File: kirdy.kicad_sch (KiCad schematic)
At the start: 14 parts, among them J11 BG050-10A-0-0650-0737-0350-L-D, J12 Kirdy LD Adapter, J13 BG050-10A-0-0650-0737-0350-L-D

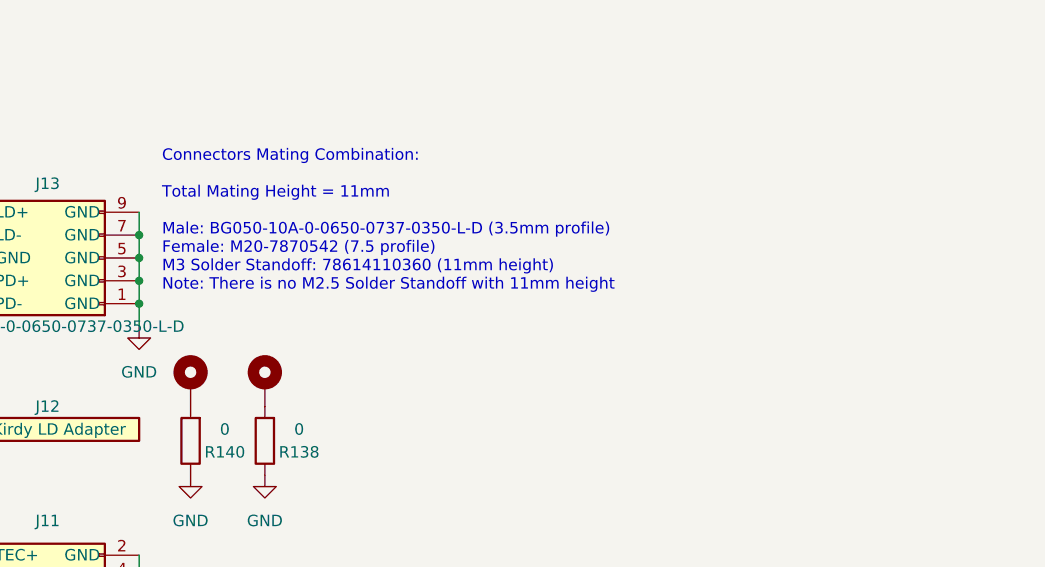
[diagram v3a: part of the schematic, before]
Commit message: sch, pcb: Add 12V & Mounting holes to MCU EXT HDR
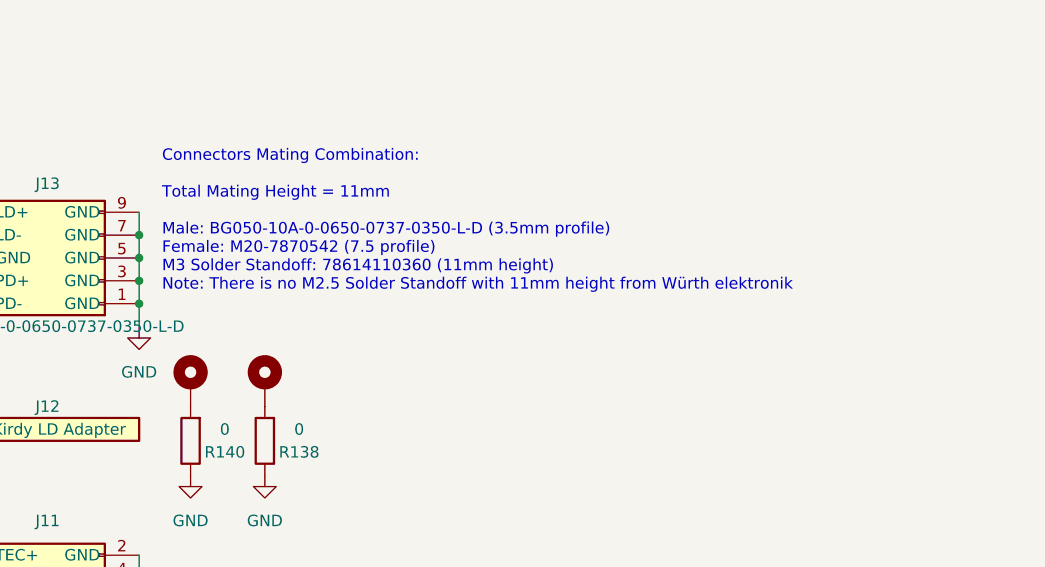
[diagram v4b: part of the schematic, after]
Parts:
- J11, J13: MFR_PN_ALT (none) -> BG050-10A-0-0450-0737-0350-L-D
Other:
- note added: "Connectors Mating Combination: Total Mating Height = 11mm Male: BG050-10A-0-0650-0737-0350-L-D (3.5mm profile) Female: M20-7870542 (7.5 profile) M3 Solder Standoff: 78614110360 (11mm height) Note: There is no M2.5 Solder Standoff with 11mm height from Würth elektronik"
- note removed: "Connectors Mating Combination: Total Mating Height = 11mm Male: BG050-10A-0-0650-0737-0350-L-D (3.5mm profile) Female: M20-7870542 (7.5 profile) M3 Solder Standoff: 78614110360 (11mm height) Note: There is no M2.5 Solder Standoff with 11mm height"
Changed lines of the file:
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@@
     (effects (font (size 2.54 2.54)) (justify left bottom))
   )
-  (text "Connectors Mating Combination:\n\nTotal Mating Height = 11mm\n\nMale: BG050-10A-0-0650-0737-0350-L-D (3.5mm profile) \nFemale: M20-7870542 (7.5 profile) \nM3 Solder Standoff: 78614110360 (11mm height)\nNote: There is no M2.5 Solder Standoff with 11mm height"
+  (text "Connectors Mating Combination:\n\nTotal Mating Height = 11mm\n\nMale: BG050-10A-0-0650-0737-0350-L-D (3.5mm profile) \nFemale: M20-7870542 (7.5 profile) \nM3 Solder Standoff: 78614110360 (11mm height)\nNote: There is no M2.5 Solder Standoff with 11mm height from Würth elektronik"
     (at 307.34 121.92 0)
     (effects (font (size 1.27 1.27)) (justify left bottom))
@@
     )
     (property "MFR_PN" "BG050-10A-0-0650-0737-0350-L-D" (at 304.8 123.19 0)
+      (effects (font (size 1.27 1.27)) hide)
+    )
+    (property "MFR_PN_ALT" "BG050-10A-0-0450-0737-0350-L-D " (at 304.8 123.19 0)
       (effects (font (size 1.27 1.27)) hide)
     )
@@
       (effects (font (size 1.27 1.27)) hide)
     )
+    (property "MFR_PN_ALT" "BG050-10A-0-0450-0737-0350-L-D " (at 284.48 151.13 0)
+      (effects (font (size 1.27 1.27)) hide)
+    )

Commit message: Cleanup and Update Modification Date
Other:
- note added: "Connectors Mating Combination: Total Mating Height = 11mm Male: BG050-10A-0-0650-0737-0350-L-D (3.5mm profile) Female: M20-7870542 (7.5mm profile) M3 Solder Standoff: 78614110360 (11mm height)"
- note removed: "Connectors Mating Combination: Total Mating Height = 11mm Male: BG050-10A-0-0650-0737-0350-L-D (3.5mm profile) Female: M20-7870542 (7.5 profile) M3 Solder Standoff: 78614110360 (11mm height) Note: There is no M2.5 Solder Standoff with 11mm height from Würth elektronik"
- note removed: "ToDo: Check all C0G New Tantalum footprints"
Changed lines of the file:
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@@
   (title_block
     (title "Kirdy")
-    (date "2023-11-09")
+    (date "2023-11-27")
     (rev "r0_3")
     (company "M-Labs Limited")
@@
     (stroke (width 0) (type default))
   )
-  (text "ToDo:\nCheck all C0G New Tantalum footprints" (at 216.535 53.975 0)
-    (effects (font (size 2.54 2.54)) (justify left bottom))
-  )
-  (text "Connectors Mating Combination:\n\nTotal Mating Height = 11mm\n\nMale: BG050-10A-0-0650-0737-0350-L-D (3.5mm profile) \nFemale: M20-7870542 (7.5 profile) \nM3 Solder Standoff: 78614110360 (11mm height)\nNote: There is no M2.5 Solder Standoff with 11mm height from Würth elektronik"
-    (at 307.34 121.92 0)
+  (text "Connectors Mating Combination:\n\nTotal Mating Height = 11mm\n\nMale: BG050-10A-0-0650-0737-0350-L-D (3.5mm profile) \nFemale: M20-7870542 (7.5mm profile) \nM3 Solder Standoff: 78614110360 (11mm height)"
+    (at 307.34 123.825 0)
     (effects (font (size 1.27 1.27)) (justify left bottom))
   )

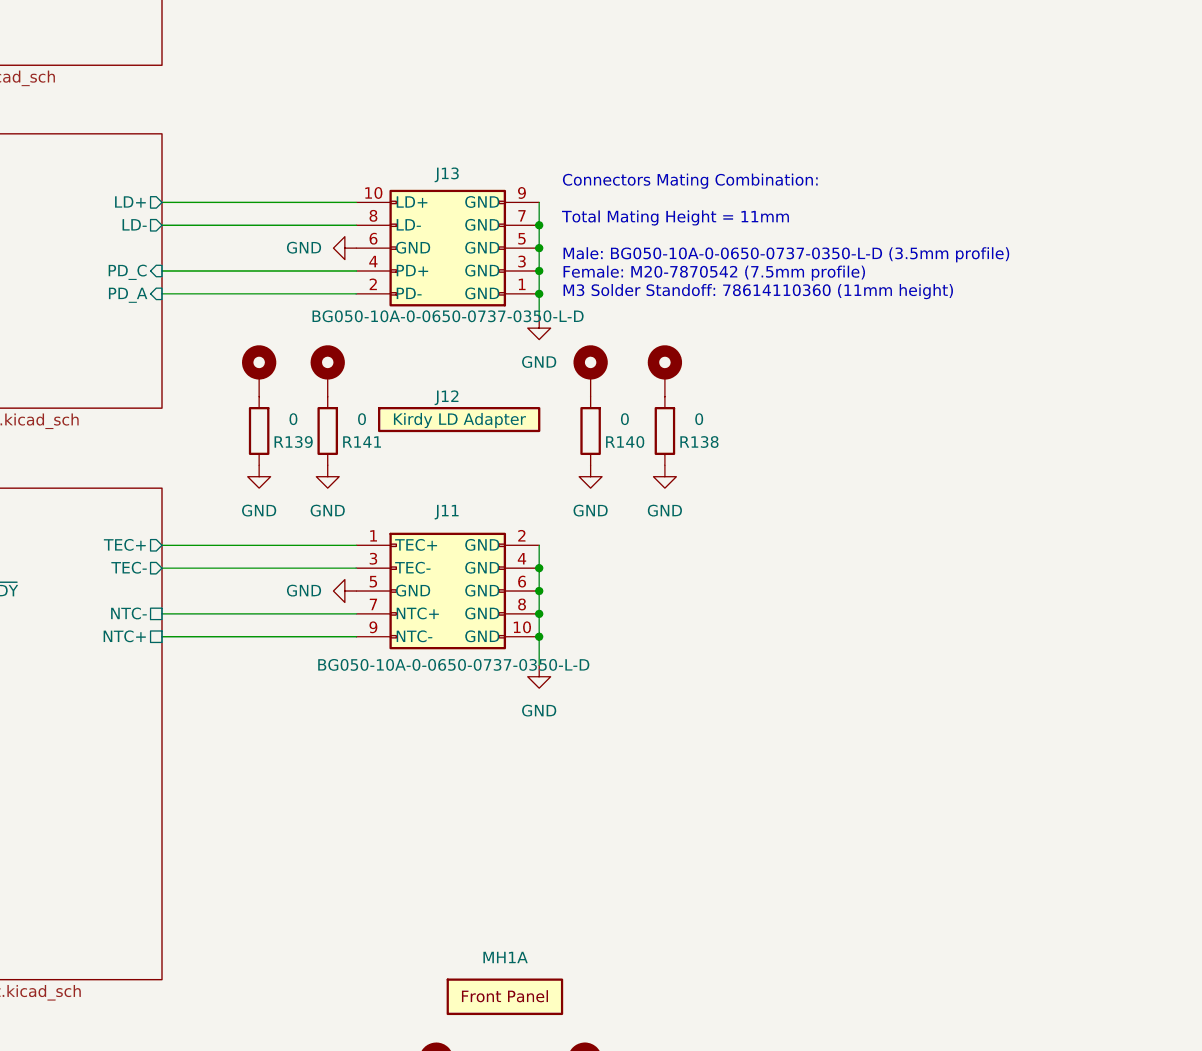
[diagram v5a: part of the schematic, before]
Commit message: sch: Add Mounting Screw Symbol and MFR/PN
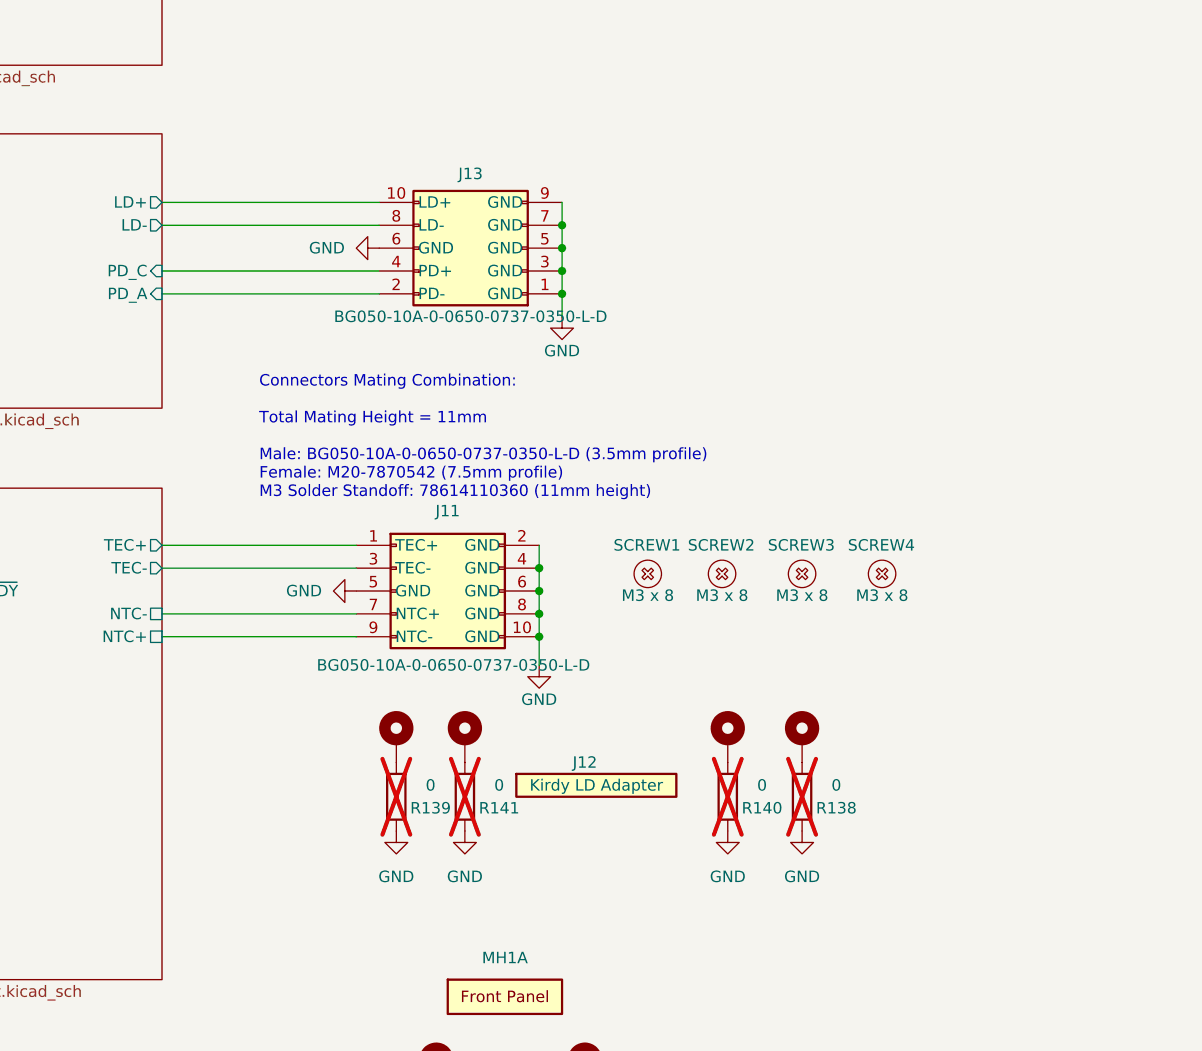
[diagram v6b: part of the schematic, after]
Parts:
- added SCREW1, SCREW2, SCREW3, SCREW4: M3 x 8, symbol kirdy:Screw
- R138, R139, R140, R141: now not fitted
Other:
- moved on the sheet: J12, J13

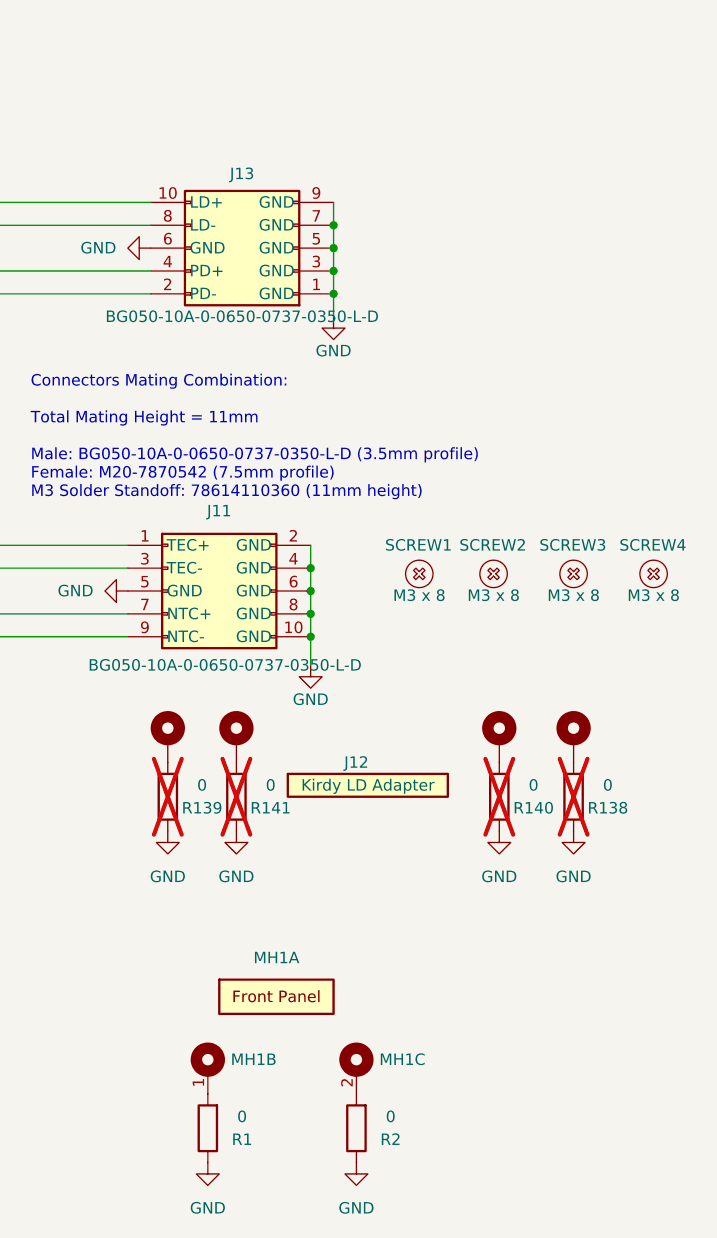
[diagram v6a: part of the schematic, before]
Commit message: Reassign Reference Designators for all Symbols
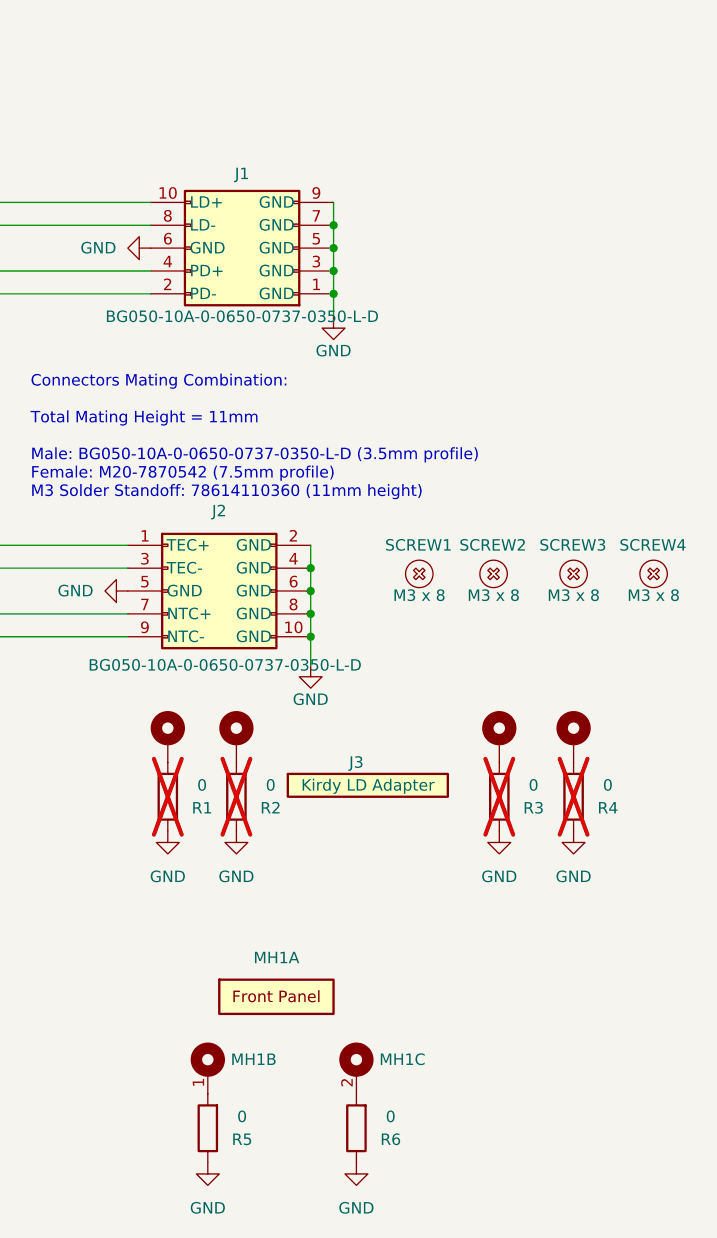
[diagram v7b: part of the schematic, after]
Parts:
- renumbered H3 to H2, H4 to H3, H2 to H4, J13 to J1, J11 to J2, J12 to J3, R139 to R1, R141 to R2, R140 to R3, R138 to R4, R1 to R5, R2 to R6

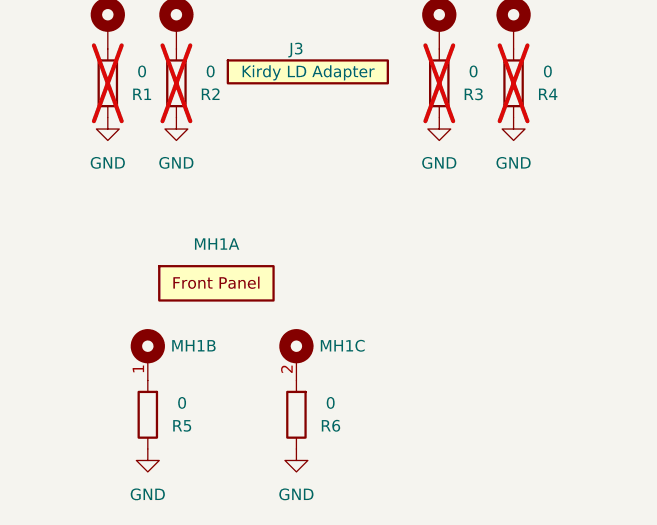
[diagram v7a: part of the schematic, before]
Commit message: Add Front Panel MFR_PN
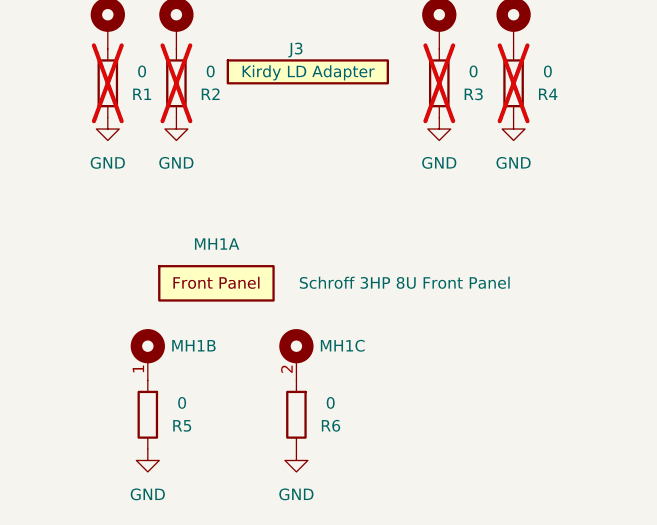
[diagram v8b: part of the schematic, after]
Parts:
- MH1: value Kirdy Front Panel -> Schroff 3HP 8U Front Panel; MFR_PN Kirdy Front Panel -> 20818022
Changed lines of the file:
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@@
       (effects (font (size 1.27 1.27)) (justify left))
     )
-    (property "Value" "Kirdy Front Panel" (at 309.88 208.28 0)
+    (property "Value" "Schroff 3HP 8U Front Panel" (at 309.88 208.28 0)
       (effects (font (size 1.27 1.27)) hide)
     )
@@
       (effects (font (size 1.27 1.27)) hide)
     )
-    (property "MFR_PN" "Kirdy Front Panel" (at 309.88 208.28 0)
+    (property "MFR_PN" "20818022" (at 309.88 208.28 0)
       (effects (font (size 1.27 1.27)) hide)
     )
@@
   )
   (symbol (lib_name "Panel_1") (lib_id "kirdy:Panel") (at 294.64 199.39 0) (unit 1)
-    (in_bom yes) (on_board yes) (dnp no) (fields_autoplaced)
+    (in_bom yes) (on_board yes) (dnp no)
     (property "Reference" "MH1" (at 300.99 196.977 0)
       (effects (font (size 1.27 1.27)))
     )
-    (property "Value" "Kirdy Front Panel" (at 294.64 199.39 0)
-      (effects (font (size 1.27 1.27)) hide)
+    (property "Value" "Schroff 3HP 8U Front Panel" (at 321.945 201.295 0)
+      (effects (font (size 1.27 1.27)))
     )
     (property "Footprint" "kirdy:Panel" (at 294.64 199.39 0)
@@
       (effects (font (size 1.27 1.27)) hide)
     )
-    (property "MFR_PN" "Kirdy Front Panel" (at 300.99 197.485 0)
+    (property "MFR_PN" "20818022" (at 300.99 197.485 0)
       (effects (font (size 1.27 1.27)) hide)
     )
@@
       (effects (font (size 1.27 1.27)) (justify left))
     )
-    (property "Value" "Kirdy Front Panel" (at 293.37 208.28 0)
+    (property "Value" "Schroff 3HP 8U Front Panel" (at 293.37 208.28 0)
       (effects (font (size 1.27 1.27)) hide)
     )
@@
       (effects (font (size 1.27 1.27)) hide)
     )
-    (property "MFR_PN" "Kirdy Front Panel" (at 293.37 208.28 0)
-      (effects (font (size 1.27 1.27)) hide)
-    )
+    (property "MFR_PN" "20818022" (at 293.37 208.28 0)
+      (effects (font (size 1.27 1.27)) hide)
+    )
